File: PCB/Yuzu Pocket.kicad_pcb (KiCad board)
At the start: 2 copper layers, 88.9 x 50.8 mm, 104 parts, among them J1 USB_A, SW1 LXW-52X52X2-SMD, SW2 LXW-52X52X2-SMD, U1 3225 24M 12PF 10PPM, U10 V3LP, U2 ULN2003, U3 USBLC6-2SC6, U4 W25Q256JVFIQT, U5 TMI3253S, U6 ULN2003, U8 ME6211C15M5, U9 ME6211C33M5

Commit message: PCB Layout + Routing Done
The business card is ready for silkscreen!
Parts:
- removed C36, C37, C38, C39, C40, C41: .1uF, Capacitor_SMD:C_0603_1608Metric_Pad1.08x0.95mm_HandSolder
- removed R2: 10k, Resistor_SMD:R_0603_1608Metric_Pad0.98x0.95mm_HandSolder
- removed SW2: LXW-52X52X2-SMD, easyeda2kicad:SW-SMD_4P-L5.2-W5.2-P5.80-LS6.4
- removed TP2: TestPoint, TestPoint:TestPoint_Pad_D1.5mm
- moved C4 241.3 mm to (168.1, 128.0), turned to 180 degrees
- moved C6 240.0 mm to (168.1, 129.5), turned to 180 degrees
- moved R3 230.4 mm to (173.0, 129.0), turned to 90 degrees
- moved R10 228.9 mm to (170.6, 129.0), turned to 90 degrees
- moved R8 226.3 mm to (165.6, 128.8), turned to 90 degrees
- moved R14 218.8 mm to (164.0, 128.8), turned to 90 degrees
- moved C12 194.9 mm to (182.1, 118.8), turned to 180 degrees
- moved U4 188.8 mm to (169.8, 121.2)
- moved C10 184.3 mm to (182.1, 117.1), turned to 180 degrees
- moved R21 182.1 mm to (186.1, 118.0), turned to 90 degrees
- moved C13 173.7 mm to (128.8, 106.7), turned to 135 degrees
- moved R23 171.5 mm to (176.6, 118.0), turned to 90 degrees
- moved R19 170.5 mm to (184.6, 118.0), turned to 90 degrees
- moved R25 169.7 mm to (178.1, 118.0), turned to 90 degrees
- moved C11 168.7 mm to (127.7, 107.7), turned to 135 degrees
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- renumbered C11 to C10, C10 to C11, C13 to C12, C12 to C13, U8 to U7, U9 to U8, U10 to U9
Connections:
- C33 pad 2: +3.3V -> +1.5V
- C34 pad 2: +1.2V -> +1.5V
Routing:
- net +5V: track 0.00 -> 167.4 mm, vias 0 -> 20
- net +3.3V: track 0.00 -> 162.7 mm, vias 0 -> 6
- net +1.2V: track 0.00 -> 95.5 mm, vias 0 -> 5
- net +1.5V: track 0.00 -> 51.9 mm, vias 0 -> 2
- net GND: track 0.00 -> 49.7 mm, vias 0 -> 36
- net Net-(D8-A): track 0.00 -> 49.2 mm
- net /DAT1: track 0.00 -> 47.9 mm, vias 0 -> 2
- net Net-(D9-A): track 0.00 -> 46.4 mm
- net /DAT0: track 0.00 -> 44.5 mm, vias 0 -> 2
- net Net-(D10-A): track 0.00 -> 43.3 mm
- net /USB D-: track 0.00 -> 42.9 mm, vias 0 -> 2
- net /USB D+: track 0.00 -> 41.6 mm, vias 0 -> 2
- net Net-(D11-A): track 0.00 -> 39.3 mm
- net /SD_CLK: track 0.00 -> 39.0 mm, vias 0 -> 2
- net /SD_CMD: track 0.00 -> 38.9 mm, vias 0 -> 2
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- added copper zone on B.Cu, net GND
- added copper zone on F.Cu, net GND
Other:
- outline, holes or cut-outs redrawn

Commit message: firmware + zine page
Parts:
- added G***: LOGO, LOGO, B.Cu at (113.7, 143.1)
- added G***: LOGO, LOGO, B.Cu at (125.6, 143.6)
- added G***: LOGO, LOGO, B.Cu at (144.7, 117.8)
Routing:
- net /LEDG4: track 16.8 -> 18.3 mm
- net /LEDG5: track 18.5 -> 19.9 mm
- net /FLASH_CLK: track 17.4 -> 16.2 mm
- net /LEDG6: track 18.0 -> 18.9 mm
- net /FLASH_DI: track 17.1 -> 17.7 mm
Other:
- board text added: "1.2V"
- board text added: "1.5V"
- board text added: "3.3V"
- board text added: "Check out how I made this!"
- board text added: "GND"
- board text added: "Logan Peterson"
- board text added: "Plug Me in!"
- board text added: "REV-1"
- board text added: "RX"
- board text added: "TX"
- board text added: "Yuzu Pocket"
- board text added: "contactloganpeterson@gmail.com loganpeterson.org github.com/sharkingstudios This card runs linux!"

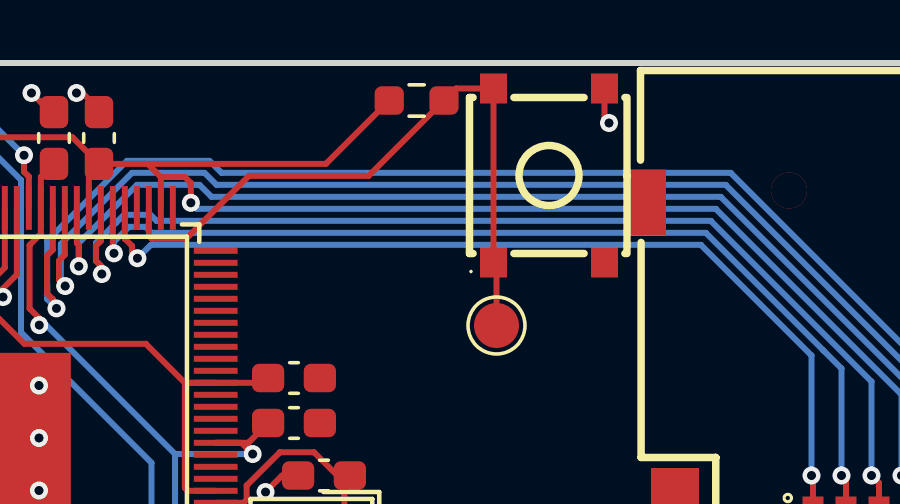
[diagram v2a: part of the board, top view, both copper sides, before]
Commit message: Updated Gerbers to V1.1 and Fleshed out README
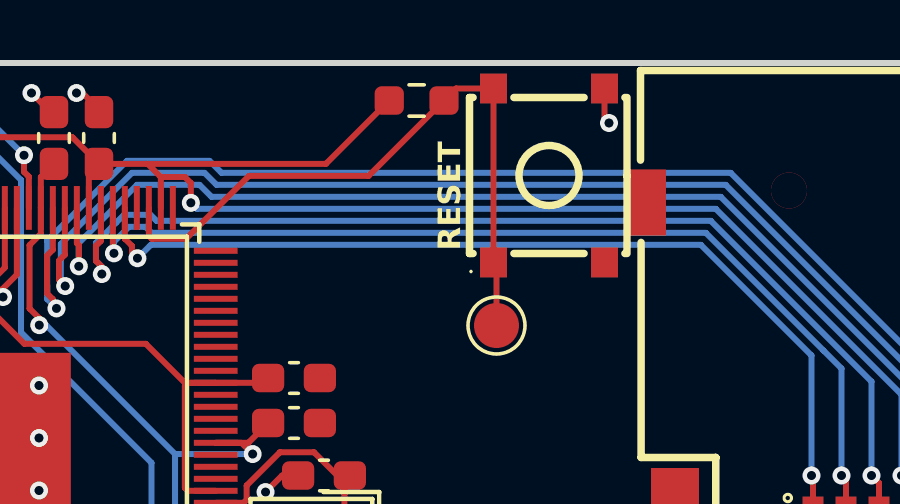
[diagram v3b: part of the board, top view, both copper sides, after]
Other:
- board text added: "RESET"
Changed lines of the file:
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@@
 		(title "Yuzu Pocket")
 		(date "2026-06-10")
-		(rev "1")
+		(rev "1.1")
 		(company "Logan Peterson")
 	)
@@
 				)
 			)
+		)
+	)
+	(gr_text "RESET"
+		(at 165.5 106.25 90)
+		(layer "F.SilkS")
+		(effects
+			(font
+				(face "Rockwell Extra Bold")
+				(size 0.75 0.75)
+				(thickness 0.1875)
+				(bold yes)
+			)
+			(justify left top)
+		)
+		(render_cache "RESET" 90
+			(polygon
+				(pts
+					(xy 166.25 105.626905) (xy 165.959839 105.782152) (xy 165.959839 105.867424) (xy 166.076938 105.867424)
+					(xy 166.076938 105.813614) (xy 166.25 105.813614) (xy 166.25 106.203883) (xy 166.076389 106.203883)
+					(xy 166.076389 106.145998) (xy 165.70778 106.145998) (xy 165.70778 106.203883) (xy 165.534856 106.203883)
+					(xy 165.534856 105.843793) (xy 165.693126 105.843793) (xy 165.693126 105.867424) (xy 165.827948 105.867424)
+					(xy 165.827948 105.83816) (xy 165.82433 105.756415) (xy 165.817489 105.735635) (xy 165.803997 105.718313)
+					(xy 165.78597 105.706928) (xy 165.760857 105.702834) (xy 165.735621 105.706912) (xy 165.717168 105.718313)
+					(xy 165.70394 105.735843) (xy 165.697064 105.757972) (xy 165.694354 105.786273) (xy 165.693126 105.843793)
+					(xy 165.534856 105.843793) (xy 165.534856 105.815125) (xy 165.536642 105.718222) (xy 165.541772 105.641789)
+					(xy 165.550747 105.583217) (xy 165.565836 105.535432) (xy 165.588882 105.49508) (xy 165.620082 105.460988)
+					(xy 165.658939 105.434607) (xy 165.70176 105.418875) (xy 165.749821 105.413498) (xy 165.786349 105.416766)
+					(xy 165.820059 105.426381) (xy 165.851578 105.442395) (xy 165.878317 105.463828) (xy 165.899317 105.488534)
+					(xy 165.915097 105.516859) (xy 166.07616 105.419772) (xy 166.07616 105.367886) (xy 166.25 105.367886)
+				)
+			)
+			(polygon
+				(pts
+					(xy 166.25 104.623434) (xy 166.25 105.306245) (xy 166.076389 105.306245) (xy 166.076389 105.250878)
+					(xy 165.70778 105.250878) (xy 165.70778 105.307253) (xy 165.534856 105.307253) (xy 165.534856 104.623434)
+					(xy 165.766078 104.623434) (xy 165.766078 104.813348) (xy 165.70778 104.813348) (xy 165.70778 104.972304)
+					(xy 165.816224 104.972304) (xy 165.816224 104.831437) (xy 165.96277 104.831437) (xy 165.96277 104.972304)
+					(xy 166.077076 104.972304) (xy 166.077076 104.813348) (xy 166.019282 104.813348) (xy 166.019282 104.623434)
+				)
+			)
+			(polygon
+				(pts
+					(xy 166.25 104.355988) (xy 166.25 104.519295) (xy 166.018457 104.519295) (xy 166.018457 104.356354)
+					(xy 166.054812 104.341521) (xy 166.080643 104.323534) (xy 166.098149 104.302597) (xy 166.108615 104.278228)
+					(xy 166.112247 104.24933) (xy 166.108877 104.222816) (xy 166.100253 104.206376) (xy 166.087021 104.196852)
+					(xy 166.067642 104.193414) (xy 166.046394 104.198204) (xy 166.028853 104.212877) (xy 166.011167 104.240717)
+					(xy 165.980905 104.303231) (xy 165.941361 104.384055) (xy 165.91267 104.43155) (xy 165.881998 104.466834)
+					(xy 165.840038 104.497588) (xy 165.808497 104.512725) (xy 165.77483 104.521832) (xy 165.738463 104.524928)
+					(xy 165.689354 104.520516) (xy 165.647851 104.508004) (xy 165.612491 104.487885) (xy 165.582255 104.459852)
+					(xy 165.557897 104.426151) (xy 165.540467 104.388938) (xy 165.529766 104.347541) (xy 165.526064 104.301079)
+					(xy 165.529492 104.254368) (xy 165.539341 104.21313) (xy 165.555241 104.176483) (xy 165.577217 104.143726)
+					(xy 165.534856 104.143726) (xy 165.534856 103.979411) (xy 165.74002 103.979411) (xy 165.74002 104.141253)
+					(xy 165.70062 104.160039) (xy 165.67502 104.183015) (xy 165.660149 104.210389) (xy 165.655024 104.243697)
+					(xy 165.658198 104.267501) (xy 165.666402 104.282454) (xy 165.679199 104.291264) (xy 165.698209 104.294484)
+					(xy 165.716728 104.290761) (xy 165.729304 104.280242) (xy 165.743006 104.25797) (xy 165.778947 104.187735)
+					(xy 165.828778 104.091797) (xy 165.855471 104.047189) (xy 165.869161 104.029592) (xy 165.88881 104.010323)
+					(xy 165.910828 103.992917) (xy 165.932957 103.979091) (xy 165.967608 103.963342) (xy 166.003917 103.953923)
+					(xy 166.042408 103.950743) (xy 166.086196 103.955001) (xy 166.12569 103.967445) (xy 166.161835 103.988124)
+					(xy 166.195274 104.017788) (xy 166.222819 104.053093) (xy 166.2425 104.092465) (xy 166.254594 104.1367)
+					(xy 166.258792 104.186865) (xy 166.255323 104.233456) (xy 166.24513 104.276793) (xy 166.228285 104.317476)
+					(xy 166.204525 104.355988)
+				)
+			)
+			(polygon
+				(pts
+					(xy 166.25 103.180691) (xy 166.25 103.863503) (xy 166.076389 103.863503) (xy 166.076389 103.808136)
+					(xy 165.70778 103.808136) (xy 165.70778 103.86451) (xy 165.534856 103.86451) (xy 165.534856 103.180691)
+					(xy 165.766078 103.180691) (xy 165.766078 103.370605) (xy 165.70778 103.370605) (xy 165.70778 103.529562)
+					(xy 165.816224 103.529562) (xy 165.816224 103.388695) (xy 165.96277 103.388695) (xy 165.96277 103.529562)
+					(xy 166.077076 103.529562) (xy 166.077076 103.370605) (xy 166.019282 103.370605) (xy 166.019282 103.180691)
+				)
+			)
+			(polygon
+				(pts
+					(xy 166.25 102.526914) (xy 166.25 102.930006) (xy 166.076389 102.930006) (xy 166.076389 102.868503)
+					(xy 165.70778 102.868503) (xy 165.70778 102.947546) (xy 165.836741 102.947546) (xy 165.836741 103.0842)
+					(xy 165.534856 103.0842) (xy 165.534856 102.374781) (xy 165.836741 102.374781) (xy 165.836741 102.511435)
+					(xy 165.70778 102.511435) (xy 165.70778 102.589975) (xy 166.076389 102.589975) (xy 166.076389 102.526914)
+				)
+			)
